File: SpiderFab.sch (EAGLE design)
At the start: 47 parts, among them IC1 SN754410, J14 5.5x2.1mm Barrel, U1 ATMEGA328, U3 MCP73831, X1 USBSMD, Y1 16MHz

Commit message: Swap 0402 caps for 0603 package.
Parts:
- C3, C6, C8: device SparkFun-Capacitors:0.1UF-0402-16V-10% -> SparkFun-Capacitors:0.1UF-0603-25V-(+80/-20%)
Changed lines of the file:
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@@
 <part name="SUPPLY2" library="SparkFun-PowerSymbols" library_urn="urn:adsk.eagle:library:530" deviceset="VCC" device=""/>
 <part name="SUPPLY3" library="SparkFun-PowerSymbols" library_urn="urn:adsk.eagle:library:530" deviceset="VCC" device=""/>
-<part name="C3" library="SparkFun-Capacitors" library_urn="urn:adsk.eagle:library:510" deviceset="0.1UF" device="-0402-16V-10%" package3d_urn="urn:adsk.eagle:package:37413/1" value="0.1uF"/>
+<part name="C3" library="SparkFun-Capacitors" library_urn="urn:adsk.eagle:library:510" deviceset="0.1UF" device="-0603-25V-(+80/-20%)" package3d_urn="urn:adsk.eagle:package:37414/1" value="0.1uF"/>
 <part name="S1" library="SparkFun-Switches" library_urn="urn:adsk.eagle:library:535" deviceset="MOMENTARY-SWITCH-SPST" device="-SMD-4.5MM" package3d_urn="urn:adsk.eagle:package:40162/1"/>
 <part name="GND6" library="SparkFun-PowerSymbols" library_urn="urn:adsk.eagle:library:530" deviceset="GND" device=""/>
@@
 <part name="SUPPLY10" library="SparkFun-PowerSymbols" library_urn="urn:adsk.eagle:library:530" deviceset="VCC" device=""/>
 <part name="C5" library="SparkFun-Capacitors" library_urn="urn:adsk.eagle:library:510" deviceset="10UF-POLAR" device="-0603-6.3V-20%(TANT)" package3d_urn="urn:adsk.eagle:package:37422/1" value="10uF"/>
-<part name="C6" library="SparkFun-Capacitors" library_urn="urn:adsk.eagle:library:510" deviceset="0.1UF" device="-0402-16V-10%" package3d_urn="urn:adsk.eagle:package:37413/1" value="0.1uF"/>
+<part name="C6" library="SparkFun-Capacitors" library_urn="urn:adsk.eagle:library:510" deviceset="0.1UF" device="-0603-25V-(+80/-20%)" package3d_urn="urn:adsk.eagle:package:37414/1" value="0.1uF"/>
 <part name="REG2" library="SparkFun-IC-Power" library_urn="urn:adsk.eagle:library:526" deviceset="V_REG_78XX" device="-TO-220" package3d_urn="urn:adsk.eagle:package:39066/1" value="12V"/>
 <part name="D2" library="SparkFun-LED" library_urn="urn:adsk.eagle:library:529" deviceset="LED" device="1206" package3d_urn="urn:adsk.eagle:package:39352/1" value="BLUE"/>
@@
 <part name="GND13" library="SparkFun-PowerSymbols" library_urn="urn:adsk.eagle:library:530" deviceset="GND" device=""/>
 <part name="C7" library="SparkFun-Capacitors" library_urn="urn:adsk.eagle:library:510" deviceset="10UF-POLAR" device="-0603-6.3V-20%(TANT)" package3d_urn="urn:adsk.eagle:package:37422/1" value="10uF"/>
-<part name="C8" library="SparkFun-Capacitors" library_urn="urn:adsk.eagle:library:510" deviceset="0.1UF" device="-0402-16V-10%" package3d_urn="urn:adsk.eagle:package:37413/1" value="0.1uF"/>
+<part name="C8" library="SparkFun-Capacitors" library_urn="urn:adsk.eagle:library:510" deviceset="0.1UF" device="-0603-25V-(+80/-20%)" package3d_urn="urn:adsk.eagle:package:37414/1" value="0.1uF"/>
 <part name="SUPPLY11" library="SparkFun-PowerSymbols" library_urn="urn:adsk.eagle:library:530" deviceset="VCC_2" device=""/>
 <part name="GND14" library="SparkFun-PowerSymbols" library_urn="urn:adsk.eagle:library:530" deviceset="GND" device=""/>

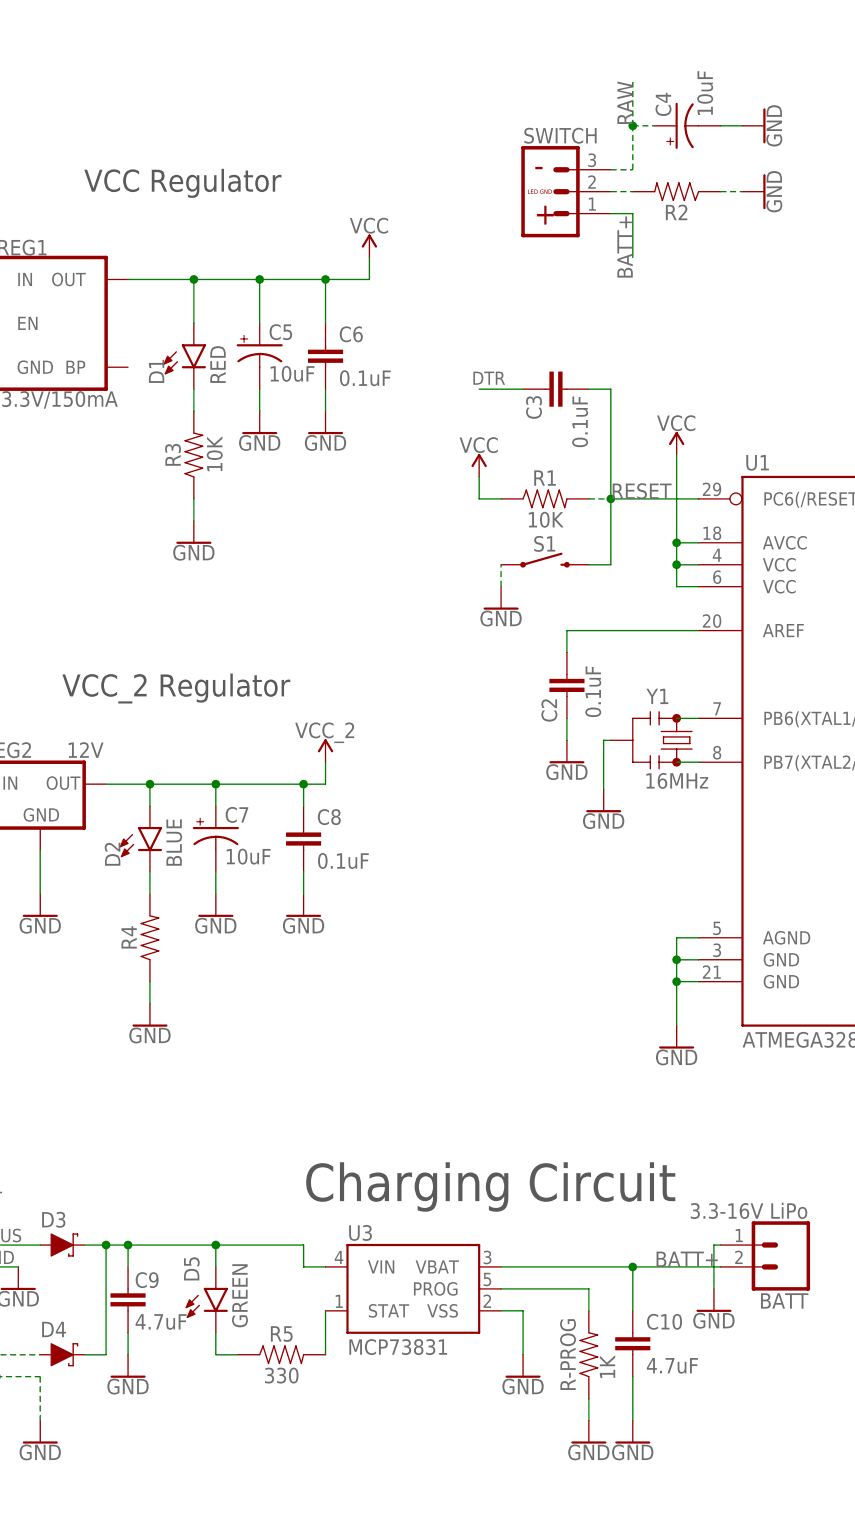
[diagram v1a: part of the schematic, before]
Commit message: Change footprint for diodes and resistors.
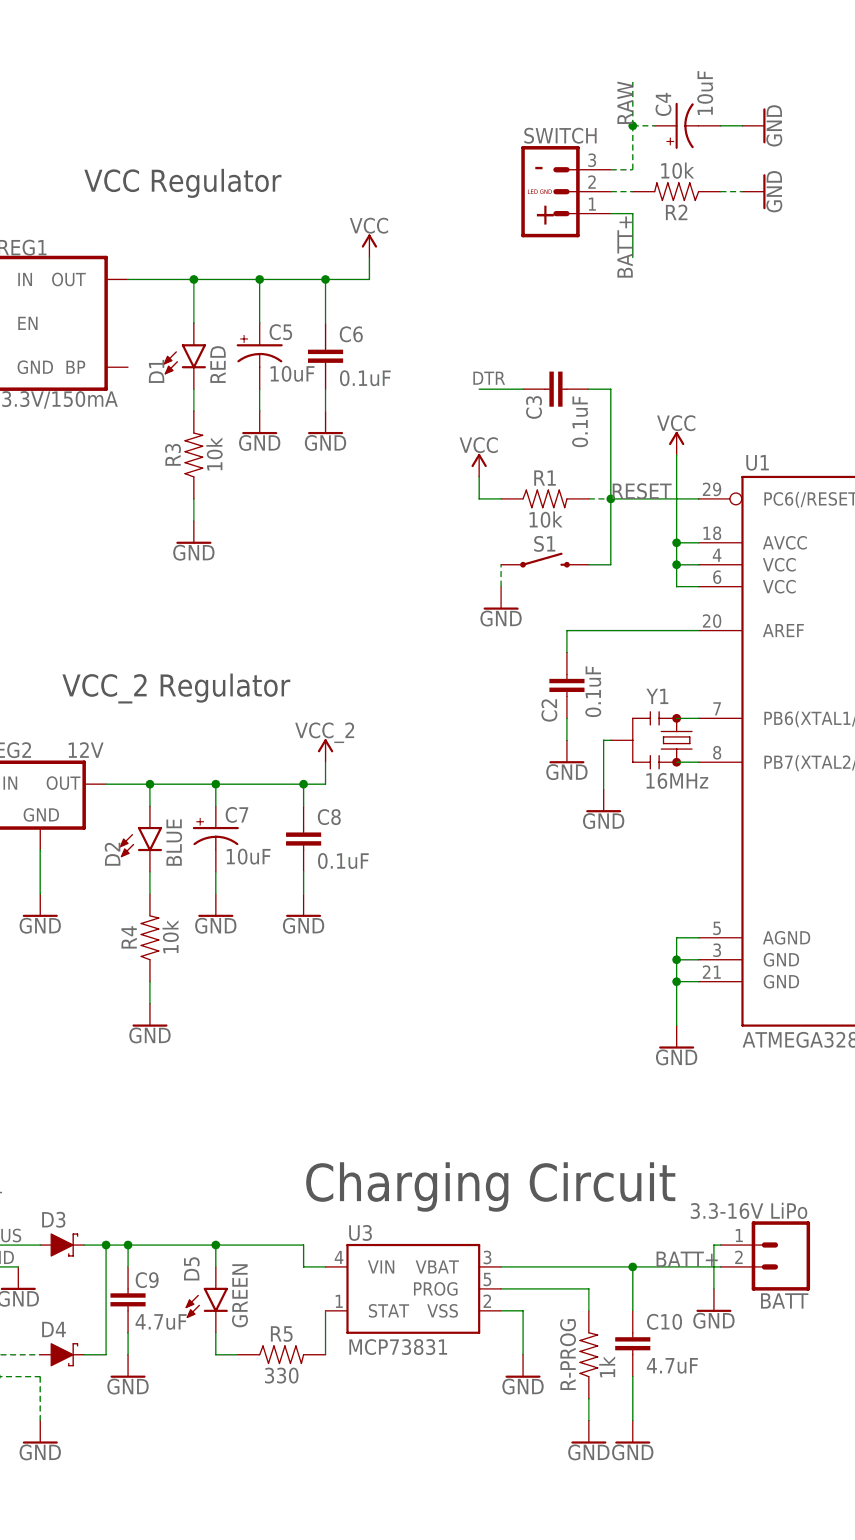
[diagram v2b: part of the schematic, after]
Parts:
- D3: device SparkFun-DiscreteSemi:DIODE-SCHOTTKY-SS14 -> SparkFun-DiscreteSemi:DIODE-SCHOTTKY-BAT20J
- R-PROG: value 1K -> 1k; device SparkFun-Resistors:RESISTOR0402 -> SparkFun-Resistors:1KOHM-0603-1/10W-1%
- R1, R3: value 10K -> 10k; device SparkFun-Resistors:RESISTOR0402 -> SparkFun-Resistors:10KOHM-0603-1/10W-1%
- R2, R4: value (none) -> 10k; device SparkFun-Resistors:RESISTOR0402 -> SparkFun-Resistors:10KOHM-0603-1/10W-1%
- R5: device SparkFun-Resistors:RESISTOR0402 -> SparkFun-Resistors:330OHM-0603-1/10W-1%
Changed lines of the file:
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@@
 <part name="S1" library="SparkFun-Switches" library_urn="urn:adsk.eagle:library:535" deviceset="MOMENTARY-SWITCH-SPST" device="-SMD-4.5MM" package3d_urn="urn:adsk.eagle:package:40162/1"/>
 <part name="GND6" library="SparkFun-PowerSymbols" library_urn="urn:adsk.eagle:library:530" deviceset="GND" device=""/>
-<part name="R1" library="SparkFun-Resistors" library_urn="urn:adsk.eagle:library:532" deviceset="RESISTOR" device="0402" package3d_urn="urn:adsk.eagle:package:39657/1" value="10K"/>
+<part name="R1" library="SparkFun-Resistors" library_urn="urn:adsk.eagle:library:532" deviceset="10KOHM" device="-0603-1/10W-1%" package3d_urn="urn:adsk.eagle:package:39650/1" value="10k"/>
 <part name="FL_A" library="SparkFun-Connectors" library_urn="urn:adsk.eagle:library:513" deviceset="CONN_03" device="" package3d_urn="urn:adsk.eagle:package:38063/1"/>
 <part name="FL_B" library="SparkFun-Connectors" library_urn="urn:adsk.eagle:library:513" deviceset="CONN_03" device="" package3d_urn="urn:adsk.eagle:package:38063/1"/>
@@
 <part name="C4" library="SparkFun-Capacitors" library_urn="urn:adsk.eagle:library:510" deviceset="10UF-POLAR" device="-0603-6.3V-20%(TANT)" package3d_urn="urn:adsk.eagle:package:37422/1" value="10uF"/>
 <part name="SWITCH" library="SparkFun-Connectors" library_urn="urn:adsk.eagle:library:513" deviceset="CONN_03" device="SCREW" package3d_urn="urn:adsk.eagle:package:38072/1"/>
-<part name="R2" library="SparkFun-Resistors" library_urn="urn:adsk.eagle:library:532" deviceset="RESISTOR" device="0402" package3d_urn="urn:adsk.eagle:package:39657/1" value=" "/>
+<part name="R2" library="SparkFun-Resistors" library_urn="urn:adsk.eagle:library:532" deviceset="10KOHM" device="-0603-1/10W-1%" package3d_urn="urn:adsk.eagle:package:39650/1" value="10k"/>
 <part name="D1" library="SparkFun-LED" library_urn="urn:adsk.eagle:library:529" deviceset="LED" device="1206" package3d_urn="urn:adsk.eagle:package:39352/1" value="RED"/>
-<part name="R3" library="SparkFun-Resistors" library_urn="urn:adsk.eagle:library:532" deviceset="RESISTOR" device="0402" package3d_urn="urn:adsk.eagle:package:39657/1" value="10K"/>
+<part name="R3" library="SparkFun-Resistors" library_urn="urn:adsk.eagle:library:532" deviceset="10KOHM" device="-0603-1/10W-1%" package3d_urn="urn:adsk.eagle:package:39650/1" value="10k"/>
 <part name="GND12" library="SparkFun-PowerSymbols" library_urn="urn:adsk.eagle:library:530" deviceset="GND" device=""/>
 <part name="SUPPLY10" library="SparkFun-PowerSymbols" library_urn="urn:adsk.eagle:library:530" deviceset="VCC" device=""/>
@@
 <part name="REG2" library="SparkFun-IC-Power" library_urn="urn:adsk.eagle:library:526" deviceset="V_REG_78XX" device="-TO-220" package3d_urn="urn:adsk.eagle:package:39066/1" value="12V"/>
 <part name="D2" library="SparkFun-LED" library_urn="urn:adsk.eagle:library:529" deviceset="LED" device="1206" package3d_urn="urn:adsk.eagle:package:39352/1" value="BLUE"/>
-<part name="R4" library="SparkFun-Resistors" library_urn="urn:adsk.eagle:library:532" deviceset="RESISTOR" device="0402" package3d_urn="urn:adsk.eagle:package:39657/1" value=" "/>
+<part name="R4" library="SparkFun-Resistors" library_urn="urn:adsk.eagle:library:532" deviceset="10KOHM" device="-0603-1/10W-1%" package3d_urn="urn:adsk.eagle:package:39650/1" value="10k"/>
 <part name="GND13" library="SparkFun-PowerSymbols" library_urn="urn:adsk.eagle:library:530" deviceset="GND" device=""/>
 <part name="C7" library="SparkFun-Capacitors" library_urn="urn:adsk.eagle:library:510" deviceset="10UF-POLAR" device="-0603-6.3V-20%(TANT)" package3d_urn="urn:adsk.eagle:package:37422/1" value="10uF"/>
@@
 <part name="J14" library="SparkFun-Connectors" library_urn="urn:adsk.eagle:library:513" deviceset="POWER_JACK" device="SMD" package3d_urn="urn:adsk.eagle:package:38221/1" value="5.5x2.1mm Barrel"/>
 <part name="U3" library="SparkFun-PowerIC" deviceset="MCP73831" device=""/>
-<part name="D3" library="SparkFun-DiscreteSemi" library_urn="urn:adsk.eagle:library:514" deviceset="DIODE-SCHOTTKY" device="-SS14" package3d_urn="urn:adsk.eagle:package:38443/1" value="1A/40V/500mV"/>
+<part name="D3" library="SparkFun-DiscreteSemi" library_urn="urn:adsk.eagle:library:514" deviceset="DIODE-SCHOTTKY" device="-BAT20J" package3d_urn="urn:adsk.eagle:package:38441/1" value="1A/40V/500mV"/>
 <part name="D4" library="SparkFun-DiscreteSemi" library_urn="urn:adsk.eagle:library:514" deviceset="DIODE-SCHOTTKY" device="-SS14" package3d_urn="urn:adsk.eagle:package:38443/1" value="1A/40V/500mV"/>
 <part name="C9" library="SparkFun-Capacitors" library_urn="urn:adsk.eagle:library:510" deviceset="4.7UF" device="0603" package3d_urn="urn:adsk.eagle:package:37414/1" value="4.7uF"/>
 <part name="C10" library="SparkFun-Capacitors" library_urn="urn:adsk.eagle:library:510" deviceset="4.7UF" device="0603" package3d_urn="urn:adsk.eagle:package:37414/1" value="4.7uF"/>
 <part name="D5" library="SparkFun-LED" library_urn="urn:adsk.eagle:library:529" deviceset="LED" device="1206" package3d_urn="urn:adsk.eagle:package:39352/1" value="GREEN"/>
-<part name="R5" library="SparkFun-Resistors" library_urn="urn:adsk.eagle:library:532" deviceset="RESISTOR" device="0402" package3d_urn="urn:adsk.eagle:package:39657/1" value="330"/>
+<part name="R5" library="SparkFun-Resistors" library_urn="urn:adsk.eagle:library:532" deviceset="330OHM" device="-0603-1/10W-1%" package3d_urn="urn:adsk.eagle:package:39650/1" value="330"/>
 <part name="GND19" library="SparkFun-PowerSymbols" library_urn="urn:adsk.eagle:library:530" deviceset="GND" device=""/>
 <part name="GND20" library="SparkFun-PowerSymbols" library_urn="urn:adsk.eagle:library:530" deviceset="GND" device=""/>
@@
 <part name="GND25" library="SparkFun-PowerSymbols" library_urn="urn:adsk.eagle:library:530" deviceset="GND" device=""/>
 <part name="GND26" library="SparkFun-PowerSymbols" library_urn="urn:adsk.eagle:library:530" deviceset="GND" device=""/>
-<part name="R-PROG" library="SparkFun-Resistors" library_urn="urn:adsk.eagle:library:532" deviceset="RESISTOR" device="0402" package3d_urn="urn:adsk.eagle:package:39657/1" value="1K"/>
+<part name="R-PROG" library="SparkFun-Resistors" library_urn="urn:adsk.eagle:library:532" deviceset="1KOHM" device="-0603-1/10W-1%" package3d_urn="urn:adsk.eagle:package:39650/1" value="1k"/>
 <part name="GND27" library="SparkFun-PowerSymbols" library_urn="urn:adsk.eagle:library:530" deviceset="GND" device=""/>
 <part name="GND28" library="SparkFun-PowerSymbols" library_urn="urn:adsk.eagle:library:530" deviceset="GND" device=""/>

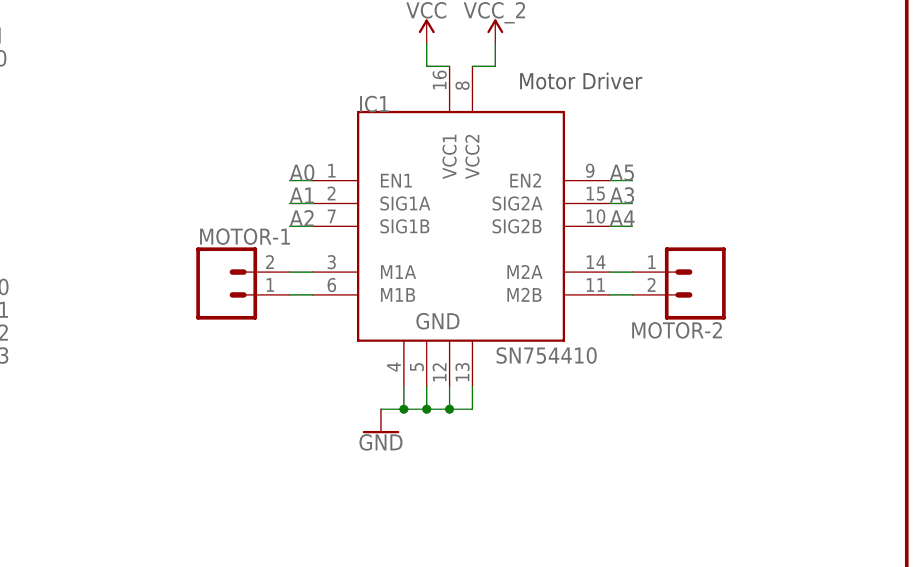
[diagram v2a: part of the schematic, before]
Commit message: Replace internal connectors with vertical JST.
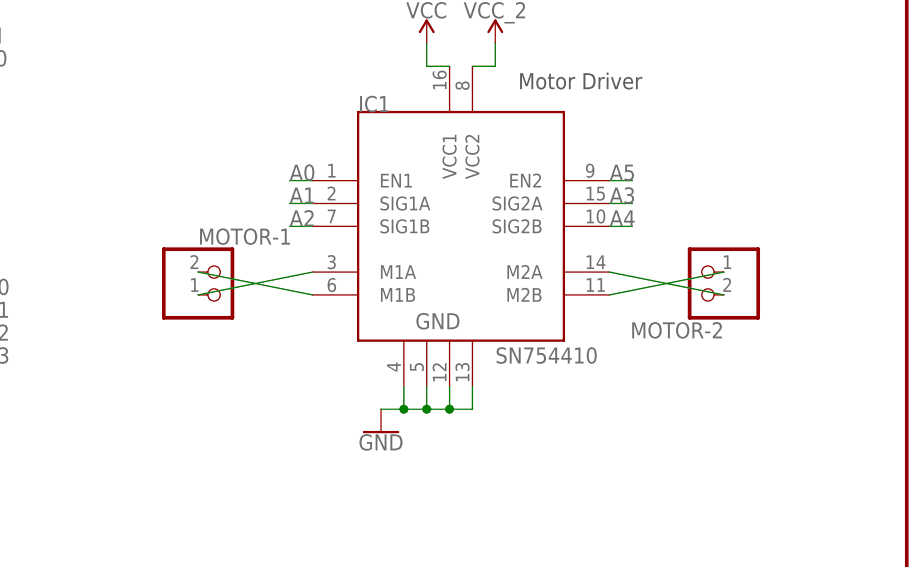
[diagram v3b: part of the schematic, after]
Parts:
- MOTOR-1, MOTOR-2: device SparkFun-Connectors:CONN_02JST-PTH-2 -> adafruit:JST_2PIN-THM
- SWITCH: device SparkFun-Connectors:CONN_03SCREW -> SparkFun-Connectors:CONN_03JST-PTH-VERT
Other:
- moved on the sheet: MOTOR-1, MOTOR-2
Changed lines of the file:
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@@
 <part name="SUPPLY8" library="SparkFun-PowerSymbols" library_urn="urn:adsk.eagle:library:530" deviceset="VCC" device=""/>
 <part name="SUPPLY9" library="SparkFun-PowerSymbols" library_urn="urn:adsk.eagle:library:530" deviceset="VCC_2" device=""/>
-<part name="MOTOR-1" library="SparkFun-Connectors" library_urn="urn:adsk.eagle:library:513" deviceset="CONN_02" device="JST-PTH-2" package3d_urn="urn:adsk.eagle:package:38053/1"/>
-<part name="MOTOR-2" library="SparkFun-Connectors" library_urn="urn:adsk.eagle:library:513" deviceset="CONN_02" device="JST-PTH-2" package3d_urn="urn:adsk.eagle:package:38053/1"/>
+<part name="MOTOR-1" library="adafruit" library_urn="urn:adsk.eagle:library:420" deviceset="JST_2PIN" device="-THM" package3d_urn="urn:adsk.eagle:package:6240693/1"/>
+<part name="MOTOR-2" library="adafruit" library_urn="urn:adsk.eagle:library:420" deviceset="JST_2PIN" device="-THM" package3d_urn="urn:adsk.eagle:package:6240693/1"/>
 <part name="REG1" library="SparkFun-IC-Power" library_urn="urn:adsk.eagle:library:526" deviceset="V_REG_MIC5205" device="3.3V" package3d_urn="urn:adsk.eagle:package:39060/1" value="3.3V/150mA"/>
 <part name="GND11" library="SparkFun-PowerSymbols" library_urn="urn:adsk.eagle:library:530" deviceset="GND" device=""/>
 <part name="C4" library="SparkFun-Capacitors" library_urn="urn:adsk.eagle:library:510" deviceset="10UF-POLAR" device="-0603-6.3V-20%(TANT)" package3d_urn="urn:adsk.eagle:package:37422/1" value="10uF"/>
-<part name="SWITCH" library="SparkFun-Connectors" library_urn="urn:adsk.eagle:library:513" deviceset="CONN_03" device="SCREW" package3d_urn="urn:adsk.eagle:package:38072/1"/>
+<part name="SWITCH" library="SparkFun-Connectors" library_urn="urn:adsk.eagle:library:513" deviceset="CONN_03" device="JST-PTH-VERT" package3d_urn="urn:adsk.eagle:package:38080/1"/>
 <part name="R2" library="SparkFun-Resistors" library_urn="urn:adsk.eagle:library:532" deviceset="10KOHM" device="-0603-1/10W-1%" package3d_urn="urn:adsk.eagle:package:39650/1" value="10k"/>
 <part name="D1" library="SparkFun-LED" library_urn="urn:adsk.eagle:library:529" deviceset="LED" device="1206" package3d_urn="urn:adsk.eagle:package:39352/1" value="RED"/>
@@
 <pinref part="IC1" gate="G$1" pin="M1A"/>
 <pinref part="MOTOR-1" gate="G$1" pin="2"/>
-<wire x1="180.34" y1="78.74" x2="182.88" y2="78.74" width="0.1524" layer="91" grouprefs="MOTORS"/>
+<wire x1="170.18" y1="76.2" x2="182.88" y2="78.74" width="0.1524" layer="91" grouprefs="MOTORS"/>
 </segment>
 </net>
@@
 <pinref part="IC1" gate="G$1" pin="M1B"/>
 <pinref part="MOTOR-1" gate="G$1" pin="1"/>
-<wire x1="180.34" y1="76.2" x2="182.88" y2="76.2" width="0.1524" layer="91" grouprefs="MOTORS"/>
+<wire x1="170.18" y1="78.74" x2="182.88" y2="76.2" width="0.1524" layer="91" grouprefs="MOTORS"/>
 </segment>
 </net>
@@
 <pinref part="IC1" gate="G$1" pin="M2A"/>
 <pinref part="MOTOR-2" gate="G$1" pin="1"/>
-<wire x1="215.9" y1="78.74" x2="218.44" y2="78.74" width="0.1524" layer="91" grouprefs="MOTORS"/>
+<wire x1="215.9" y1="78.74" x2="228.6" y2="76.2" width="0.1524" layer="91" grouprefs="MOTORS"/>
 </segment>
 </net>
@@
 <pinref part="IC1" gate="G$1" pin="M2B"/>
 <pinref part="MOTOR-2" gate="G$1" pin="2"/>
-<wire x1="215.9" y1="76.2" x2="218.44" y2="76.2" width="0.1524" layer="91" grouprefs="MOTORS"/>
-</segment>
-</net>
+<wire x1="215.9" y1="76.2" x2="228.6" y2="78.74" width="0.1524" layer="91" grouprefs="MOTORS"/>
+</segment>
+</net>
